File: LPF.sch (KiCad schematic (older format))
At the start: 139 parts, among them J1 Conn_02x05_Counter_Clockwise, P1 SMA, P3 SMA, P4 SMA

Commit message: trace cleaning, SMA edge added, main connector rotated
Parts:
- added P2, P5, P6: SMA, Connector_Coaxial:SMA_Amphenol_132289_EdgeMount, symbol BNC
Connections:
- net GND: now also P2.2 (Ext), P5.2 (Ext), P6.2 (Ext)
- net at P3.1 (In), RL10.8, RL10.9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: now also P6.1 (In)
- net at P1.1 (In), RL1.8, RL1.9: now also P2.1 (In)
- net at P4.1 (In), RL1.11, RL1.6: now also P5.1 (In)
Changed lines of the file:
@@
 	0    -1   -1   0
 $EndComp
+$Comp
+L BNC P5
+U 1 1 5A2FBDFF
+P 800 5000
+F 0 "P5" H 810 5120 50  0000 C CNN
+F 1 "SMA" V 910 4940 50  0000 C CNN
+F 2 "Connector_Coaxial:SMA_Amphenol_132289_EdgeMount" H 800 5000 50  0001 C CNN
+F 3 "" H 800 5000 50  0000 C CNN
+	1    800  5000
+	-1   0    0    -1
+$EndComp
+$Comp
+L GND #PWR099
+U 1 1 5A2FBE05
+P 800 5250
+F 0 "#PWR099" H 800 5000 50  0001 C CNN
+F 1 "GND" H 800 5100 50  0000 C CNN
+F 2 "" H 800 5250 50  0000 C CNN
+F 3 "" H 800 5250 50  0000 C CNN
+	1    800  5250
+	1    0    0    -1
+$EndComp
+Text Notes -150 3550 0    39   ~ 0
+To 15 W PA output\n
+Wire Wire Line
+	800  5200 800  5250
+$Comp
+L BNC P2
+U 1 1 5A2FC218
+P 800 4400
+F 0 "P2" H 810 4520 50  0000 C CNN
+F 1 "SMA" V 910 4340 50  0000 C CNN
+F 2 "Connector_Coaxial:SMA_Amphenol_132289_EdgeMount" H 800 4400 50  0001 C CNN
+F 3 "" H 800 4400 50  0000 C CNN
+	1    800  4400
+	-1   0    0    -1
+$EndComp
+$Comp
+L GND #PWR0100
+U 1 1 5A2FC21E
+P 800 4650
+F 0 "#PWR0100" H 800 4400 50  0001 C CNN
+F 1 "GND" H 800 4500 50  0000 C CNN
+F 2 "" H 800 4650 50  0000 C CNN
+F 3 "" H 800 4650 50  0000 C CNN
+	1    800  4650
+	1    0    0    -1
+$EndComp
+Wire Wire Line
+	800  4600 800  4650
+Wire Wire Line
+	950  5000 950  4900
+Connection ~ 950  4900
+Wire Wire Line
+	950  4400 950  4300
+Connection ~ 950  4300
+$Comp
+L BNC P6
+U 1 1 5A2FD79F
+P 7550 5000
+F 0 "P6" H 7560 5120 50  0000 C CNN
+F 1 "SMA" H 7750 5000 50  0000 C CNN
+F 2 "Connector_Coaxial:SMA_Amphenol_132289_EdgeMount" H 7550 5000 50  0001 C CNN
+F 3 "" H 7550 5000 50  0000 C CNN
+	1    7550 5000
+	1    0    0    -1
+$EndComp
+$Comp
+L GND #PWR0101
+U 1 1 5A2FD7A5
+P 7550 5250
+F 0 "#PWR0101" H 7550 5000 50  0001 C CNN
+F 1 "GND" H 7550 5100 50  0000 C CNN
+F 2 "" H 7550 5250 50  0000 C CNN
+F 3 "" H 7550 5250 50  0000 C CNN
+	1    7550 5250
+	1    0    0    -1
+$EndComp
+$Comp
+L GND #PWR0102
+U 1 1 5A2FD7AB
+P 7550 5250
+F 0 "#PWR0102" H 7550 5000 50  0001 C CNN
+F 1 "GND" H 7550 5100 50  0000 C CNN
+F 2 "" H 7550 5250 50  0000 C CNN
+F 3 "" H 7550 5250 50  0000 C CNN
+	1    7550 5250
+	1    0    0    -1
+$EndComp
+Wire Wire Line
+	7550 5200 7550 5250
+Connection ~ 7400 5000
 $EndSCHEMATC

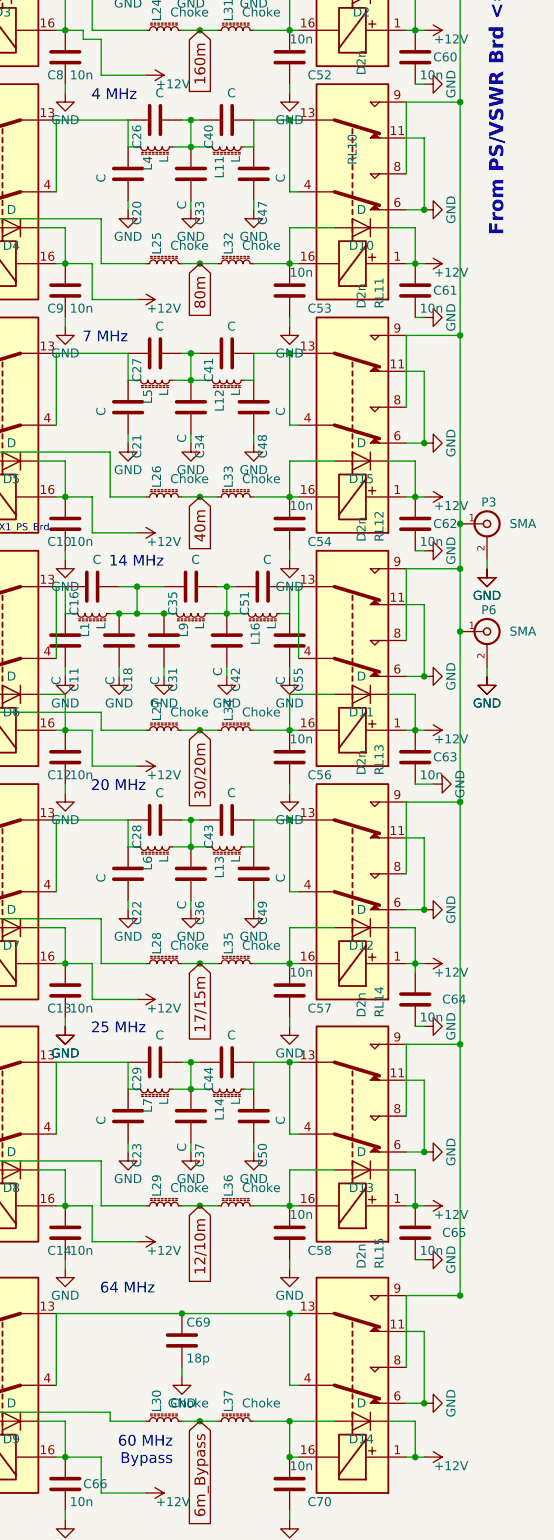
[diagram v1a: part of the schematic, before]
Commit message: changed sma footprint, gerber done
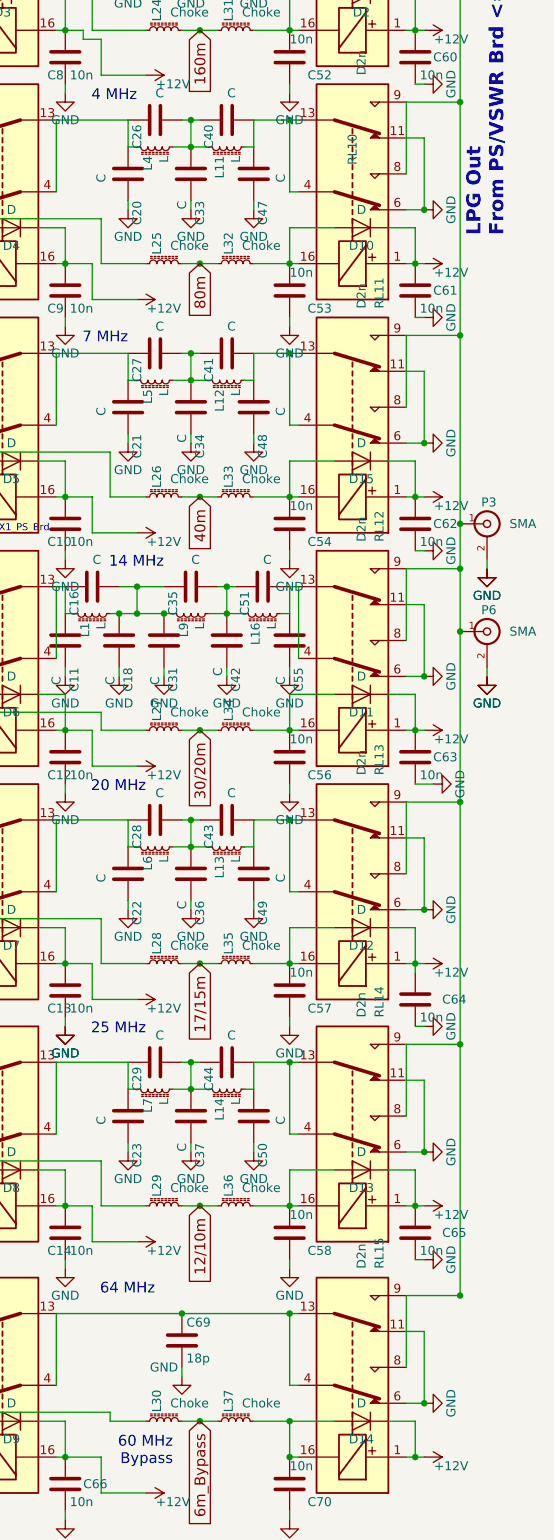
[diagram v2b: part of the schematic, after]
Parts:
- P2, P5, P6: footprint Connector_Coaxial:SMA_Amphenol_132289_EdgeMount -> SMA_PINS:SMA_EDGE_NRW
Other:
- note added: "LPG Out\nFrom PS/VSWR Brd <== TX Conn Brd"
- note removed: "From PS/VSWR Brd <== TX Conn Brd"
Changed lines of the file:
@@
 To 15 W PA output\n
 Text Notes 7650 2800 1    79   ~ 16
-From PS/VSWR Brd <== TX Conn Brd
+LPG Out\nFrom PS/VSWR Brd <== TX Conn Brd
 $Comp
 L +12V #PWR075
@@
 P 5850 9150
 F 0 "#PWR082" H 5850 8900 50  0001 C CNN
-F 1 "GND" H 5850 9000 50  0000 C CNN
+F 1 "GND" H 5750 9200 50  0000 C CNN
 F 2 "" H 5850 9150 50  0000 C CNN
 F 3 "" H 5850 9150 50  0000 C CNN
@@
 F 0 "P5" H 810 5120 50  0000 C CNN
 F 1 "SMA" V 910 4940 50  0000 C CNN
-F 2 "Connector_Coaxial:SMA_Amphenol_132289_EdgeMount" H 800 5000 50  0001 C CNN
+F 2 "SMA_PINS:SMA_EDGE_NRW" H 800 5000 50  0001 C CNN
 F 3 "" H 800 5000 50  0000 C CNN
 	1    800  5000
@@
 F 0 "P2" H 810 4520 50  0000 C CNN
 F 1 "SMA" V 910 4340 50  0000 C CNN
-F 2 "Connector_Coaxial:SMA_Amphenol_132289_EdgeMount" H 800 4400 50  0001 C CNN
+F 2 "SMA_PINS:SMA_EDGE_NRW" H 800 4400 50  0001 C CNN
 F 3 "" H 800 4400 50  0000 C CNN
 	1    800  4400
@@
 F 0 "P6" H 7560 5120 50  0000 C CNN
 F 1 "SMA" H 7750 5000 50  0000 C CNN
-F 2 "Connector_Coaxial:SMA_Amphenol_132289_EdgeMount" H 7550 5000 50  0001 C CNN
+F 2 "SMA_PINS:SMA_EDGE_NRW" H 7550 5000 50  0001 C CNN
 F 3 "" H 7550 5000 50  0000 C CNN
 	1    7550 5000

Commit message: stitching and new gerber
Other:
- note added: "To RX HPF board\n"
- note removed: "To RX Conn Brd\n"
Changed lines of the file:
@@
 TX_RX_RLY
 Text Notes 850  6100 0    39   ~ 0
-To RX Conn Brd\n
+To RX HPF board\n
 Text Notes 600  4100 0    39   ~ 0
 To 15 W PA output\n

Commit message: BOM added, new Gerber
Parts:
- C11, C27: value C -> 120p
- C16, C18, C29, C41: value C -> 39p
- C17: value 24p -> 4.7p
- C19: value C -> 1000p
- C20, C25: value C -> 470p
- C21: value C -> 330p
- C22, C50, C55: value C -> 82p
- C23, C40: value C -> 68p
- C24: value 31p -> 56p
- C26: value C -> 240p
- C28: value C -> 56p
- C30: value 15p -> 12p
- C31, C35, C36: value C -> 220p
- C32: value C -> 2200p
- C33, C46: value C -> 1100p
- C34: value C -> 680p
- C37, C42: value C -> 180p
- C38: value 68p -> 56p
- C39, C51: value C -> 150p
- C43: value C -> 22p
- C44: value C -> 6.8p
- C45: value 4.7 -> 4.7p
- C47: value C -> 560p
- C48: value C -> 390p
- C49: value C -> 100p
- C59: value 24p -> C
- L1: value L -> 562nH
- L10: value L -> 4.4uH
- L11: value L -> 2.02uH
- L12: value L -> 1.36uH
- L13: value L -> 251nH
- L15, L2: value L -> 169nH
- L16, L6, L9: value L -> 311nH
- L3: value L -> 3.5uH
- L4: value L -> 1,66uHL
- L5: value L -> 1.18uH
- L8: value L -> 196nH

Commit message: chasing routing errors
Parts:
- L13: value 251nH -> 351nH
- L14: value L -> 311nH
- L7: value L -> 235nH
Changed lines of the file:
@@
 P 3250 4700
 F 0 "C38" V 3300 4850 50  0000 L CNN
-F 1 "56p" V 3200 4850 50  0000 L CNN
+F 1 "56p" V 3200 4800 50  0000 L CNN
 F 2 "ATC_B:ATC_500_HandSoldering" H 3288 4550 50  0001 C CNN
 F 3 "" H 3250 4700 50  0001 C CNN
@@
 U 1 1 592DB31D
 P 2900 4700
-F 0 "C24" V 2950 4850 50  0000 L CNN
-F 1 "56p" V 2750 4700 50  0000 L CNN
+F 0 "C24" V 2800 4850 50  0000 L CNN
+F 1 "56p" V 2950 4750 50  0000 L CNN
 F 2 "ATC_B:ATC_500_HandSoldering" H 2938 4550 50  0001 C CNN
 F 3 "" H 2900 4700 50  0001 C CNN
@@
 P 6100 6200
 F 0 "L13" H 6150 6240 50  0000 L CNN
-F 1 "251nH" H 6150 6150 50  0000 L CNN
+F 1 "351nH" H 6150 6150 50  0000 L CNN
 F 2 "T50:T50_V_THT" H 6100 6200 50  0001 C CNN
 F 3 "" H 6100 6200 50  0000 C CNN
@@
 P 6100 7550
 F 0 "L14" H 6150 7590 50  0000 L CNN
-F 1 "L" H 6150 7500 50  0000 L CNN
+F 1 "311nH" H 6150 7500 50  0000 L CNN
 F 2 "T50:T50_V_THT" H 6100 7550 50  0001 C CNN
 F 3 "" H 6100 7550 50  0000 C CNN
@@
 P 5700 7550
 F 0 "L7" H 5750 7590 50  0000 L CNN
-F 1 "L" H 5750 7500 50  0000 L CNN
+F 1 "235nH" H 5750 7500 50  0000 L CNN
 F 2 "T50:T50_V_THT" H 5700 7550 50  0001 C CNN
 F 3 "" H 5700 7550 50  0000 C CNN
